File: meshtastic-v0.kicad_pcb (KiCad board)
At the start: 2 copper layers, 71 x 46 mm, 88 parts, among them J1 USB_C_Receptacle_USB2.0_16P, J2 Conn_01x02_Pin, J3 Conn_Coaxial, J4 Conn_Coaxial, Q1 SI2302, Q2 Q_PNP_BEC, Q3 Q_NPN_BEC, U1 DM-OLED096-636, U10 LIS3DSHTR, U2 ATGM336H, U3 TPS62046DGQR, U4 HT-RA62, U5 Lever Switch TMHU26, U6 BQ24072RGT, U7 ESP32-S3-WROOM-1, U8 AT24C32A, U9 BME280

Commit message: vib motor
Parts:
- removed IO7: IO7, TestPoint:TestPoint_Pad_1.0x1.0mm
- added D9: 1N5819WS, Diode_SMD:D_SOD-323, F.Cu at (141.8, 91.5)
- added JP1: SolderJumper_2_Open, Jumper:SolderJumper-2_P1.3mm_Open_Pad1.0x1.5mm, B.Cu at (149.4, 90.7)
- added Q4: SI2302, Package_TO_SOT_SMD:SOT-23, F.Cu at (141.9, 94.5)
- added R23: 10k, Resistor_SMD:R_0805_2012Metric, F.Cu at (139.2, 93.2)
- moved R11 0.21 mm to (136.5, 93.5)
- moved R20 0.20 mm to (136.5, 95.6)
- moved Q1 0.10 mm to (136.7, 90.5)
- renumbered B to BOOT1, CLK to CLK1, CSN to CSN1, G to G1, G to G2, MISO to MISO1, MOSI to MOSI1, R to RST1, SDA to SDA1, SLC to SLC1, VS to VS1
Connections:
- U7 pad 7: /Microcontroller/IO7 -> /Microcontroller/VIB_MTR
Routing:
- net /Accelerometer/SDA: track 86.1 -> 70.5 mm
- net +3V3: track 183.2 -> 192.4 mm, vias 18 -> 21
- net /Microcontroller/VIB_MTR: track 0.00 -> 4.13 mm, vias 0 -> 1
- net /Microcontroller/BOOT: track 45.8 -> 42.2 mm
- net /Microcontroller/IO7: track 3.11 -> 0.00 mm, vias 1 -> 0
- net Net-(D9-A): track 0.00 -> 2.58 mm
- net Net-(D5-A): track 12.4 -> 14.5 mm
- net /Accelerometer/SCL: track 82.8 -> 81.1 mm, vias 6 -> 7
- net GND: vias 288 -> 272

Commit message: added vib motor fix
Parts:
- moved IO07 1.95 mm to (125.3, 92.4)
- turned R23 to 90 degrees
- renumbered IO15 to IO07
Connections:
- IO07 pad 1: /Microcontroller/IO15 -> /Microcontroller/IO07
- U7 pad 7: /Microcontroller/VIB_MTR -> /Microcontroller/IO07
- U7 pad 8: /Microcontroller/IO15 -> /Microcontroller/VIB_MTR
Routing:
- net /Accelerometer/SDA: track 70.5 -> 89.6 mm, vias 5 -> 7
- net /Microcontroller/VIB_MTR: track 4.13 -> 19.7 mm, vias 1 -> 2
- net Net-(D9-A): track 2.58 -> 11.9 mm, vias 0 -> 3
- net /Accelerometer/SCL: track 81.1 -> 87.4 mm, vias 7 -> 8
- net /Microcontroller/IO15: track 3.41 -> 0.00 mm, vias 1 -> 0
- net /Microcontroller/IO07: track 0.00 -> 3.18 mm, vias 0 -> 1
- net GND: vias 272 -> 276

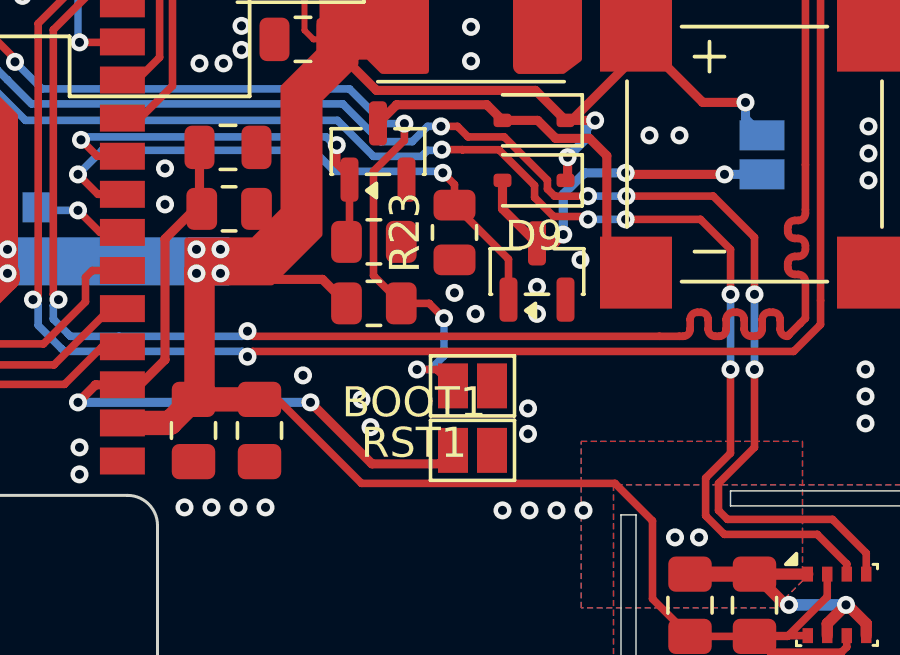
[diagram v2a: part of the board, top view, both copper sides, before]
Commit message: pcb render update
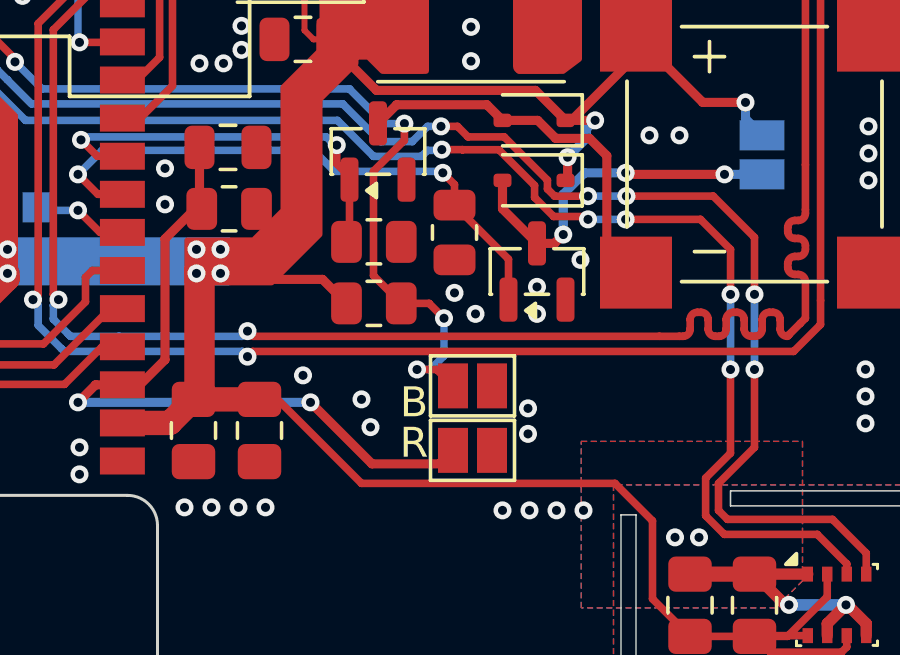
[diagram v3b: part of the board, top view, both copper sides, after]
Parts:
- renumbered BOOT1 to B, CLK1 to CLK, CSN1 to CSN, G2 to G, G1 to G, IO07 to IO7, MISO1 to MISO, MOSI1 to MOSI, RST1 to R, SLC1 to SCL, SDA1 to SDA, VS1 to VS
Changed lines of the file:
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@@
 		(descr "SMD Solder Jumper, 1x1.5mm Pads, 0.3mm gap, open")
 		(tags "solder jumper open")
-		(property "Reference" "RST1"
+		(property "Reference" "R"
 			(at 1.95 0.25 180)
 			(layer "F.SilkS" knockout)
@@
 			(at 0 -1.85 0)
 			(layer "F.SilkS")
+			(hide yes)
 			(effects
 				(font
@@
 		(descr "SMD Solder Jumper, 1x1.5mm Pads, 0.3mm gap, open")
 		(tags "solder jumper open")
-		(property "Reference" "BOOT1"
+		(property "Reference" "B"
 			(at 1.95 -0.55 180)
 			(layer "F.SilkS" knockout)
@@
 			(at 0 -1.65 90)
 			(layer "F.SilkS")
+			(hide yes)
 			(effects
 				(font
@@
 		(descr "SMD rectangular pad as test Point, square 1.0mm side length")
 		(tags "test point SMD pad rectangle square")
-		(property "Reference" "G2"
+		(property "Reference" "G"
 			(at 0 1.448 0)
 			(layer "B.SilkS" knockout)
@@
 		(descr "SMD rectangular pad as test Point, square 1.0mm side length")
 		(tags "test point SMD pad rectangle square")
-		(property "Reference" "MISO1"
+		(property "Reference" "MISO"
 			(at 2.65 0 0)
 			(layer "B.SilkS" knockout)
@@
 		(descr "SMD rectangular pad as test Point, square 1.0mm side length")
 		(tags "test point SMD pad rectangle square")
-		(property "Reference" "CLK1"
+		(property "Reference" "CLK"
 			(at 2.25 0 0)
 			(layer "B.SilkS" knockout)
@@
 		(descr "SMD rectangular pad as test Point, square 1.0mm side length")
 		(tags "test point SMD pad rectangle square")
-		(property "Reference" "G1"
+		(property "Reference" "G"
 			(at 0 1.5 0)
 			(layer "B.SilkS" knockout)
@@
 		(descr "SMD rectangular pad as test Point, square 1.0mm side length")
 		(tags "test point SMD pad rectangle square")
-		(property "Reference" "CSN1"
+		(property "Reference" "CSN"
 			(at 2.4 0 0)
 			(layer "B.SilkS" knockout)
@@
 		(descr "SMD rectangular pad as test Point, square 1.0mm side length")
 		(tags "test point SMD pad rectangle square")
-		(property "Reference" "IO07"
+		(property "Reference" "IO7"
 			(at 2.55 0 0)
 			(layer "B.SilkS" knockout)
@@
 		(descr "SMD rectangular pad as test Point, square 1.0mm side length")
 		(tags "test point SMD pad rectangle square")
-		(property "Reference" "MOSI1"
+		(property "Reference" "MOSI"
 			(at 2.65 0 0)
 			(layer "B.SilkS" knockout)
@@
 		(descr "SMD rectangular pad as test Point, square 1.0mm side length")
 		(tags "test point SMD pad rectangle square")
-		(property "Reference" "SDA1"
+		(property "Reference" "SDA"
 			(at -0.75 -1.7 0)
 			(layer "B.SilkS" knockout)
@@
 		(descr "SMD rectangular pad as test Point, square 1.0mm side length")
 		(tags "test point SMD pad rectangle square")
-		(property "Reference" "VS1"
+		(property "Reference" "VS"
 			(at 0 1.5 180)
 			(layer "B.SilkS" knockout)
@@
 		(descr "SMD rectangular pad as test Point, square 1.0mm side length")
 		(tags "test point SMD pad rectangle square")
-		(property "Reference" "SLC1"
+		(property "Reference" "SCL"
 			(at 0.6 -1.7 0)
 			(layer "B.SilkS" knockout)
@@
 	)
 	(zone
-		(net "+3V3")
-		(layer "F.Cu")
-		(hatch none 0.1)
-		(priority 30056)
-		(attr
-			(teardrop
-				(type padvia)
-			)
-		)
-		(connect_pads yes
-			(clearance 0)
-		)
-		(min_thickness 0.0254)
-		(fill yes
-			(island_removal_mode 1)
-		)
-		(polygon
-			(pts
-				(xy 142.818173 91.324833) (xy 143.122973 91.324833) (xy 143.268006 90.766558) (xy 142.970573 90.723833)
-				(xy 142.67314 90.766558)
-			)
-		)
-	)
-	(zone
 		(net "Net-(D9-A)")
 		(layer "F.Cu")
@@
 	)
 	(zone
-		(net "/LORA/SPI2_MOSI")
-		(layer "B.Cu")
-		(hatch none 0.1)
-		(priority 30075)
-		(attr
-			(teardrop
-				(type padvia)
-			)
-		)
-		(connect_pads yes
-			(clearance 0)
-		)
-		(min_thickness 0.0254)
-		(fill yes
-			(island_removal_mode 1)
-		)
-		(polygon
-			(pts
-				(xy 113.256273 92.123332) (xy 113.076668 91.943727) (xy 112.587868 92.287868) (xy 112.7415 92.4585)
-				(xy 113.092205 92.432059)
-			)
-		)
-	)
-	(zone
 		(net "/Power Management/PGOOD")
 		(layer "B.Cu")
@@
 		(layer "B.Cu")
 		(hatch none 0.1)
-		(priority 30009)
+		(priority 30000)
 		(attr
 			(teardrop
@@
 		(layer "B.Cu")
 		(hatch none 0.1)
-		(priority 30002)
+		(priority 30000)
 		(attr
 			(teardrop
@@
 		(layer "B.Cu")
 		(hatch none 0.1)
-		(priority 30007)
+		(priority 30000)
 		(attr
 			(teardrop
@@
 		(layer "B.Cu")
 		(hatch none 0.1)
-		(priority 30004)
+		(priority 30000)
 		(attr
 			(teardrop
@@
 	)
 	(zone
-		(net "/LORA/SPI2_MISO")
-		(layer "B.Cu")
-		(hatch none 0.1)
-		(priority 30053)
-		(attr
-			(teardrop
-				(type padvia)
-			)
-		)
-		(connect_pads yes
-			(clearance 0)
-		)
-		(min_thickness 0.0254)
-		(fill yes
-			(island_removal_mode 1)
-		)
-		(polygon
-			(pts
-				(xy 113.312251 94.067354) (xy 113.132646 93.887749) (xy 112.685195 94.122836) (xy 112.797478 94.402522)
-				(xy 113.077164 94.514805)
-			)
-		)
-	)
-	(zone
 		(net "/Power Management/BUCK_EN")
 		(layer "B.Cu")
@@
 		(layer "B.Cu")
 		(hatch none 0.1)
-		(priority 30008)
+		(priority 30000)
 		(attr
 			(teardrop
@@
 		(layer "B.Cu")
 		(hatch none 0.1)
-		(priority 30001)
+		(priority 30000)
 		(attr
 			(teardrop
@@
 	)
 	(zone
-		(net "/LORA/SPI2_CS_N")
-		(layer "B.Cu")
-		(hatch none 0.1)
-		(priority 30035)
-		(attr
-			(teardrop
-				(type padvia)
-			)
-		)
-		(connect_pads yes
-			(clearance 0)
-		)
-		(min_thickness 0.0254)
-		(fill yes
-			(island_removal_mode 1)
-		)
-		(polygon
-			(pts
-				(xy 113.527 96.202567) (xy 113.273 96.202567) (xy 113.122836 96.685195) (xy 113.4 96.803567) (xy 113.677164 96.685195)
-			)
-		)
-	)
-	(zone
 		(net "/Connectors/D+")
 		(layer "B.Cu")
@@
 	)
 	(zone
-		(net "/LORA/SPI2_CLK")
-		(layer "B.Cu")
-		(hatch none 0.1)
-		(priority 30056)
-		(attr
-			(teardrop
-				(type padvia)
-			)
-		)
-		(connect_pads yes
-			(clearance 0)
-		)
-		(min_thickness 0.0254)
-		(fill yes
-			(island_removal_mode 1)
-		)
-		(polygon
-			(pts
-				(xy 113.212251 90.167354) (xy 113.032646 89.987749) (xy 112.585195 90.222836) (xy 112.697478 90.502522)
-				(xy 112.977164 90.614805)
-			)
-		)
-	)
-	(zone
 		(net "/GPS/GPS_RST")
 		(layer "B.Cu")
@@
 		(layer "B.Cu")
 		(hatch none 0.1)
-		(priority 30003)
+		(priority 30000)
 		(attr
 			(teardrop
@@
 	)
 	(zone
-		(net "/Accelerometer/SCL")
-		(layer "B.Cu")
-		(hatch none 0.1)
-		(priority 30040)
-		(attr
-			(teardrop
-				(type padvia)
-			)
-		)
-		(connect_pads yes
-			(clearance 0)
-		)
-		(min_thickness 0.0254)
-		(fill yes
-			(island_removal_mode 1)
-		)
-		(polygon
-			(pts
-				(xy 117.973 85.397433) (xy 118.227 85.397433) (xy 118.377164 84.914805) (xy 118.1 84.796433) (xy 117.822836 84.914805)
-			)
-		)
-	)
-	(zone
 		(net "/Microcontroller/IO47")
 		(layer "B.Cu")
 		(hatch none 0.1)
-		(priority 30006)
+		(priority 30000)
 		(attr
 			(teardrop
@@
 			)
 		)
-	)
-	(zone
-		(net "/Accelerometer/SDA")
-		(layer "B.Cu")
-		(hatch none 0.1)
-		(priority 30044)
-		(attr
-			(teardrop
-				(type padvia)
-			)
-		)
-		(connect_pads yes
-			(clearance 0)
-		)
-		(min_thickness 0.0254)
-		(fill yes
-			(island_removal_mode 1)
-		)
-		(polygon
-			(pts
-				(xy 119.973 85.497433) (xy 120.227 85.497433) (xy 120.377164 85.014805) (xy 120.1 84.896433) (xy 119.822836 85.014805)
-			)
-		)
-	)
-	(zone
-		(net "VSYS")
-		(layer "B.Cu")
-		(hatch none 0.1)
-		(priority 30045)
-		(attr
-			(teardrop
-				(type padvia)
-			)
-		)
-		(connect_pads yes
-			(clearance 0)
-		)
-		(min_thickness 0.0254)
-		(fill yes
-			(island_removal_mode 1)
-		)
-		(polygon
-			(pts
-				(xy 135.527 79.702567) (xy 135.273 79.702567) (xy 135.122836 80.185195) (xy 135.4 80.303567) (xy 135.677164 80.185195)
-			)
-		)
